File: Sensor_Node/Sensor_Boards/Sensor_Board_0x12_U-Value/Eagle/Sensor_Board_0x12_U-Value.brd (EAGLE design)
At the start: 55 x 35 mm, 28 parts, among them IC1 MCP3911A0-E/SS, IC2 4066D, J2 ARDUINO_ISP, J4 1x3 RA Female .1", J5 1x3 RA Female .1", U2 ATMEGA328P_TQFP, Y1 8MHZ

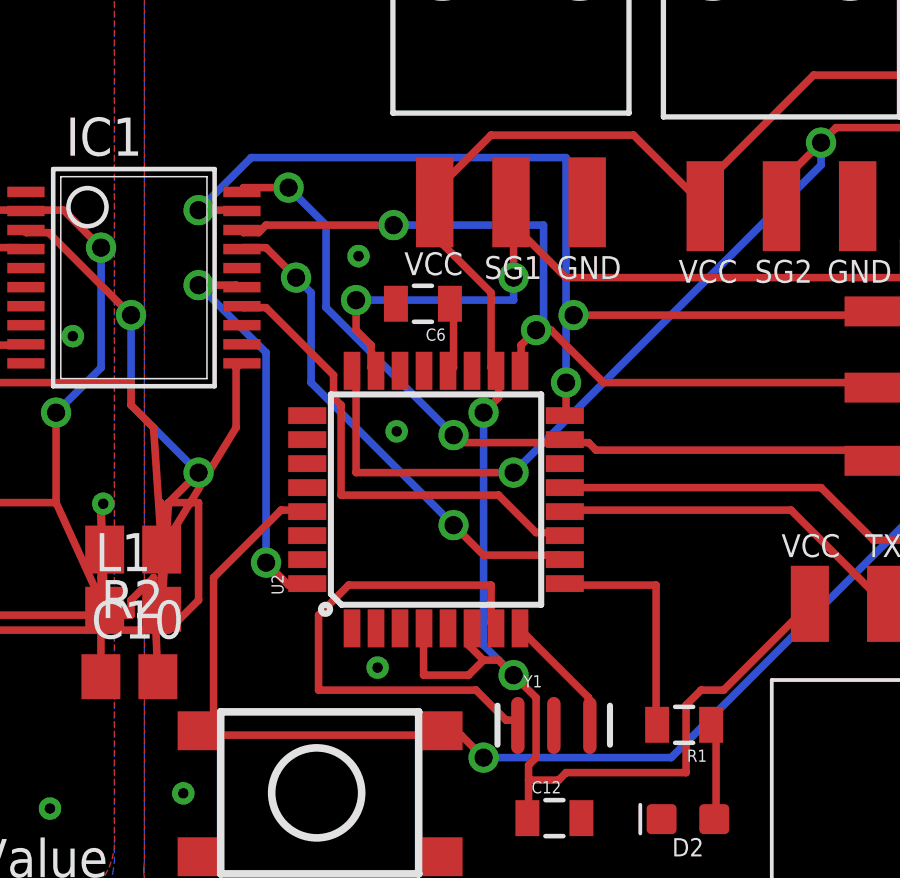
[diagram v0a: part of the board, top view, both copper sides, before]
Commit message: Renamed U-value sensor board files
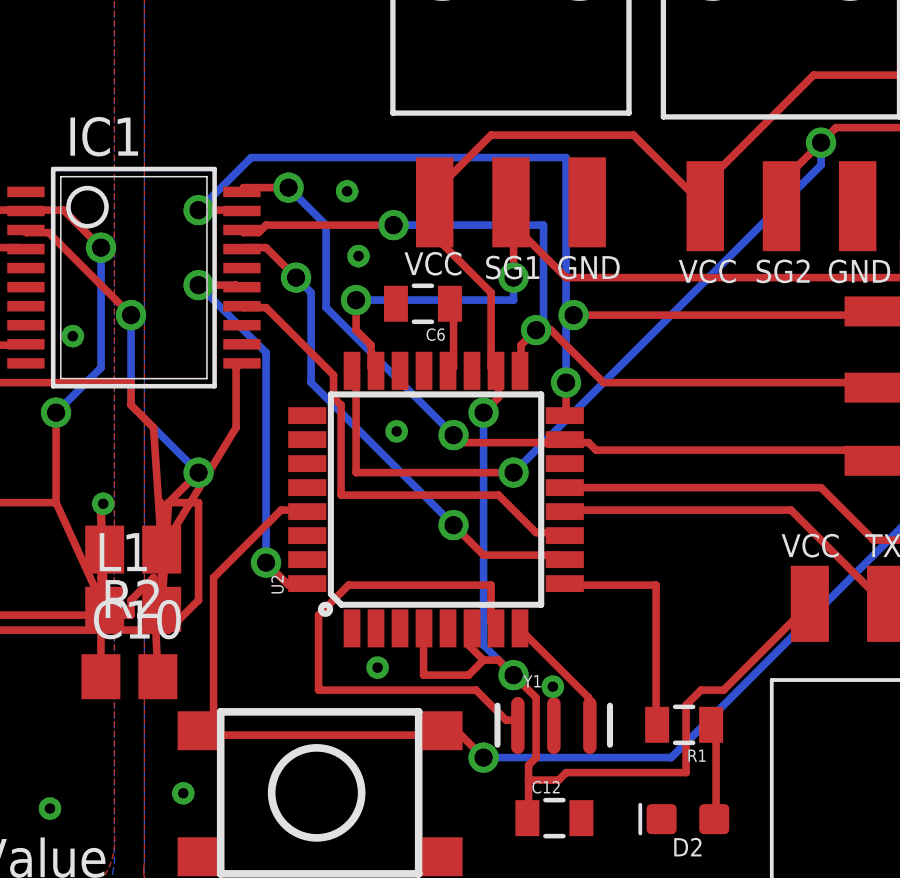
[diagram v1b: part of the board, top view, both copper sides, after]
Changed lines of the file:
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@@
 <via x="29.083" y="21.717" extent="1-16" drill="0.35"/>
 <via x="29.718" y="8.001" extent="1-16" drill="0.35"/>
-<wire x1="35.593" y1="6.071" x2="36.511" y2="2.983" width="0" layer="19" extent="1-1"/>
-<wire x1="30.353" y1="15.875" x2="30.4655" y2="9.3089" width="0" layer="19" extent="1-1"/>
+<via x="28.702" y="23.876" extent="1-16" drill="0.35"/>
+<via x="35.56" y="7.366" extent="1-16" drill="0.35"/>
+<wire x1="35.593" y1="6.071" x2="35.56" y2="7.366" width="0" layer="19" extent="1-1"/>
 </signal>
 <signal name="N$6">

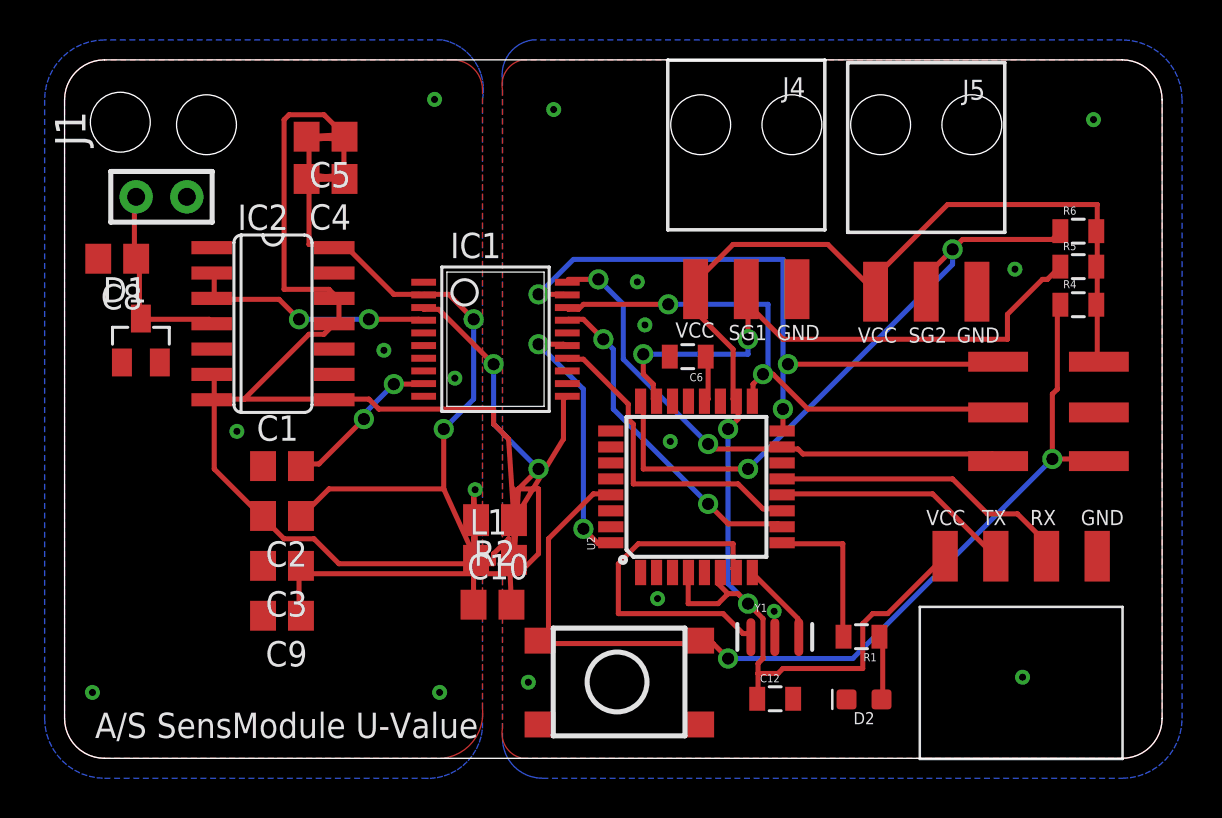
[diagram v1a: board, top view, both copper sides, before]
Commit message: Renamed Heat_Flux to U-Value
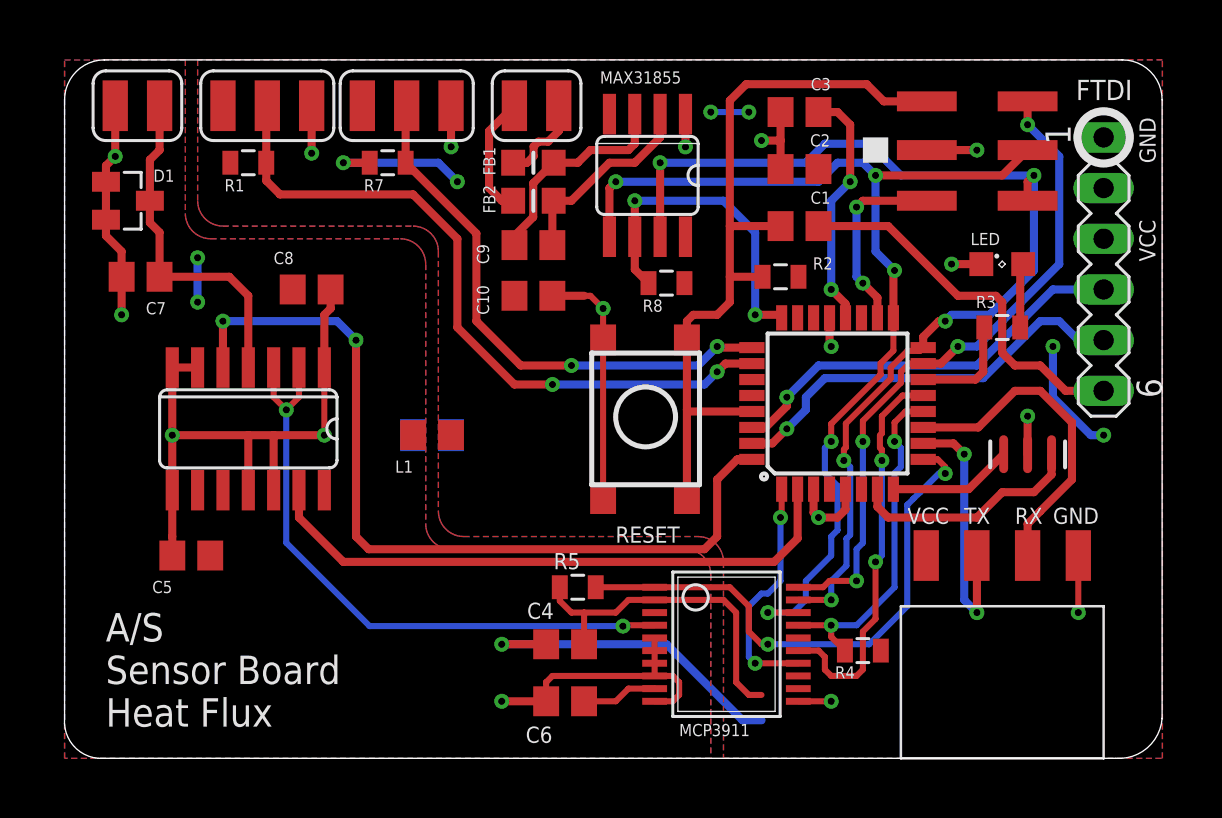
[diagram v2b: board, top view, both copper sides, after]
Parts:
- removed C12: (no value), wsn:0805
- removed D2: (no value), wsn:LED-0603
- removed J2: ARDUINO_ISP, wsn:M-2X3
- removed J5: 1x3 RA Female .1", wsn:1X03_SMD_RA_FEMALE
- removed S3: PUSHBUTTON, wsn:M-PUSHBUTTON-SMD
- removed U$1: M04_SMD_90, wsn:M04_SMD_90
- added C7: 1u, eagle-ltspice:C0805
- added FB1, FB2: (no value), Adafruit_MAX31855 v2:MICROBUILDER__0805MP
- added IC4: MAX31855, Adafruit_MAX31855 v2:ADAFRUIT_SO08
- added LED: Red, led:SML0805
- added PAD1, PAD10, PAD2, PAD3, PAD4, PAD5, PAD6, PAD7, PAD8, PAD9: WIREPADSMD1,27-254, wirepad:SMD1,27-2,54
- added R3: 330, SparkFun-Passives:0805
- added R7, R8: 10k, SparkFun-Passives:0805
- added S1: Reset, marc_library:M-PUSHBUTTON-SMD
- added SV1: (no value), con-lstb:MA06-1
- C1, C2, C3, C4, C5: device heatflow:C0805 -> eagle-ltspice:C0805
- C10, C8: value 1u -> 100n; device heatflow:C0805 -> eagle-ltspice:C0805
- C6: value (none) -> 100n; device wsn:0805 -> eagle-ltspice:C0805
- C9: value 100n -> 10n; device heatflow:C0805 -> eagle-ltspice:C0805
- D1: value BAV99 -> LEDXLAMP_BAV99; device LEDXLamp:SOT23 -> Sensor_Board_0x07_Heat_Flux:LEDXLAMP_SOT23
- IC1: value MCP3911A0-E/SS -> MCP3911; device heatflow:SSOP20 -> Sensor_Board_0x07_Heat_Flux:HEATFLOW_SSOP20
- IC2: value 4066D -> 40XX_4066D; device 40xx:SO14 -> Sensor_Board_0x07_Heat_Flux:40XX_SO14
- J1: value (none) -> M04_SMD_90; device Stecker_Pins:CON2X1 -> myownthings:M04_SMD_90
- J4: value 1x3 RA Female .1" -> ARDUINO_ISP; device wsn:1X03_SMD_RA_FEMALE -> marc_library:M-2X3
- L1: value 74279220601 -> HEATFLOW2_74279220601; device heatflow2:0805 -> Sensor_Board_0x07_Heat_Flux:HEATFLOW2_0805
- R1: value 330 -> 10k; device wsn:0805 -> SparkFun-Passives:0805
- R2: value 0 -> 10k; device resistor:M0805 -> SparkFun-Passives:0805
- R4: value 100k -> 10k; device wsn:0805 -> SparkFun-Passives:0805
- R5: value 4.7K -> 10k; device wsn:0805 -> SparkFun-Passives:0805
- R6: value 4.7K -> 0; device wsn:0805 -> Sensor_Board_0x07_Heat_Flux:RESISTOR_M0805
- U2: device wsn:TQFP32-08 -> marc_library:TQFP32-08
- Y1: device wsn:RESONATOR-SMD -> marc_library:RESONATOR-SMD
- moved J1 41.2 mm to (43.2, 10.2), turned to 0 degrees
- moved R1 38.8 mm to (9.21, 29.8)
- moved C3 34.5 mm to (36.8, 32.4)
- moved R6 34.0 mm to (18.4, 16.2), flipped to the bottom
- moved C2 31.2 mm to (36.8, 29.5)
- moved R5 29.8 mm to (25.7, 8.57), turned to 180 degrees
- moved C4 28.8 mm to (25.1, 2.86), turned to 0 degrees
- moved C1 28.6 mm to (36.8, 26.7), turned to 180 degrees
- moved C9 22.4 mm to (23.5, 25.7), turned to 0 degrees
- moved C5 22.0 mm to (6.35, 10.2)
- moved R4 20.4 mm to (40.0, 5.40)
- moved IC1 19.2 mm to (33.0, 5.71)
- moved R2 18.8 mm to (35.9, 24.1), turned to 0 degrees
- moved C6 15.7 mm to (25.1, 5.71)
- moved Y1 15.6 mm to (48.3, 15.2), turned to 180 degrees
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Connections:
- removed net ADCLK: IC1.15, U2.32
- removed net AD_CS: IC1.17, U2.10
- removed net AD_RESET: IC1.1
- removed net AVDD: C3.1, C9.1, IC1.3, L1.2
- removed net D10_SS: U2.14
- removed net DATA_READY: IC1.14, U2.11
- removed net DS18B20_1: J4.2, R5.1, U2.23
- removed net DS18B20_2: J5.2, R6.1, U2.24
- removed net DVDD: C10.1, C2.1, C4.1, C5.1, IC1.2, IC2.14, L1.1
- removed net GND: C12.2, C6.2, D2.C, J2.P$5, J5.1, S3.1, S3.2, U2.21, U2.3, U2.5, Y1.2
- removed net LED: R1.2, U2.9
- removed net N$10: U2.28
- removed net N$11: U2.19
- removed net N$12: C8.1, D1.3, IC2.4, J1.2
- removed net N$13: U2.22
- removed net N$17: U2.1
- removed net N$18: U2.2
- removed net N$2 (its old number): C1.2, IC1.9
- removed net N$24: D2.A, R1.1
- removed net SHORT: IC2.13
- removed net VCC: C12.1, J2.P$6, J4.3, J5.3, R4.2, R5.2, R6.2, U$1.1, U2.18, U2.4, U2.6
- new net AVCC: C5.1, C8.1, IC1.3, IC2.14, L1.2
- new net DS18B20_DATA_1: PAD4.1, R1.1, U2.26
- new net DS18B20_DATA_2: PAD7.1, R7.1, U2.25
- new net DVCC: C10.1, C2.1, C6.1, IC1.2, IC4.4, J1.1, J4.P$6, L1.1, PAD3.1, PAD6.1, R1.2, R2.2, R4.2, R5.2, R7.2, R8.2, SV1.3, U2.18, U2.4, U2.6
- new net FTDI_RESET: C1.1, SV1.6
- new net INPUT_SHORT: IC2.13, U2.2
- new net L1: R3.2, U2.14
- new net MAX_CS: IC4.6, R8.1, U2.24
- new net MCP_CLK: IC1.15, U2.13
- new net MCP_CS: IC1.17, R4.1, U2.12
- new net MCP_DATA_RDY: IC1.14, U2.1
- new net MCP_RESET: IC1.1, R5.1, U2.9
- new net N$30: LED.A, R3.1
- new net N$8: C9.2, FB2.2, IC4.2
- net AGND: now also C4.1, C5.2, C7.2, IC2.11, IC2.12, IC2.6, IC2.7, IC2.8, PAD2.1, R6.2; no longer C1.1, C3.2, C9.2, J1.1, R2.2
- net DGND: now also C3.2, C6.2, IC4.1, J1.4, J4.P$5, LED.C, PAD5.1, PAD8.1, R6.1, S1.1, S1.2, SV1.1, SV1.2, U2.21, U2.3, U2.5, Y1.2; no longer C4.2, C5.2, IC2.11, IC2.12, IC2.6, IC2.7, IC2.8, R2.1
- net FTDI_RXI: now also SV1.4, U2.30; no longer U2.31
- net FTDI_TXO: now also SV1.5, U2.31; no longer U2.30
- net INPUT_EN: now also U2.32
- net MCU_RXI: now also J1.3, U2.11; no longer U$1.3, U2.13
- net MCU_TXO: now also J1.2, U2.10; no longer U$1.2, U2.12
- net MISO: now also IC4.7, J4.P$1; no longer J2.P$1
- net MOSI: now also J4.P$3; no longer J2.P$3
- net N$15: now also C3.1, U2.20; no longer J4.1
- net N$3: now also FB1.1, PAD9.1; no longer C6.1, U2.20
- net N$4: now also C4.2, IC1.9; no longer U$1.4
- net N$6: now also C7.1, D1.3, IC2.4, PAD1.1; no longer U2.25
- net N$7: now also FB2.1, PAD10.1; no longer U2.26
- net N$9: now also C9.1, FB1.2, IC4.3; no longer U2.27
- net RESET: now also C1.2, J4.P$4, R2.1, S1.3, S1.4; no longer J2.P$4, R4.1, S3.3, S3.4
- net SCK: now also IC4.5, J4.P$2; no longer J2.P$2
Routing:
- net VCC: track 74.9 -> 0.00 mm, vias 2 -> 0
- net AGND: track 0.00 -> 56.5 mm, vias 7 -> 5
- net DVDD: track 50.3 -> 0.00 mm, vias 2 -> 0
- net INPUT_EN: track 0.00 -> 42.9 mm, vias 0 -> 2
- net DVCC: track 0.00 -> 41.8 mm, vias 0 -> 8
- net AVDD: track 38.7 -> 0.00 mm, vias 2 -> 0
- net DS18B20_DATA_1: track 0.00 -> 35.4 mm, vias 0 -> 2
- net DS18B20_2: track 32.4 -> 0.00 mm, vias 2 -> 0
- net DS18B20_1: track 30.6 -> 0.00 mm, vias 2 -> 0
- net INPUT_SHORT: track 0.00 -> 30.2 mm
- net DGND: track 82.7 -> 55.0 mm, vias 0 -> 13
- net MCP_RESET: track 0.00 -> 27.6 mm, vias 0 -> 2
- net DS18B20_DATA_2: track 0.00 -> 27.4 mm, vias 0 -> 2
- net SCK: track 28.0 -> 52.4 mm, vias 2 -> 5
- net FTDI_RXI: track 0.00 -> 21.1 mm, vias 0 -> 1
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- added copper zone on layer 1, net AVCC
- added copper zone on layer 16, net DGND
- added copper zone on layer 1, net DVCC
- removed copper zone on layer 1, net AGND
- removed copper zone on layer 1, net GND
- removed copper zone on layer 16, net GND
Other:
- outline, holes or cut-outs redrawn
- board text added: "A/S Sensor Board Heat Flux"
- board text added: "DATA"
- board text added: "DS18B20"
- board text added: "FTDI"
- board text added: "IN1"
- board text added: "IN2"
- board text added: "MAX31855"
- board text added: "MCP3911"
- board text added: "RESET"
- board text added: "T-COUPLE"
- board text added: "UIN"
- board text added: "uV Input"
- board text removed: "A/S SensModule U-Value"
- board text removed: "SG1"
- board text removed: "SG2"
